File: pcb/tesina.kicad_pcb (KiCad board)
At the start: 2 copper layers, 70 x 35 mm, 73 parts, among them J1 PWR_IN, J2 AMP1_IN, J3 AMP1_OUT2, J4 AMP1_OUT1, J5 AMP2_IN, J6 AMP3_IN, J7 AMP2_OUT, J8 AMP3_OUT, Q1 BFP640, Q2 BFP640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

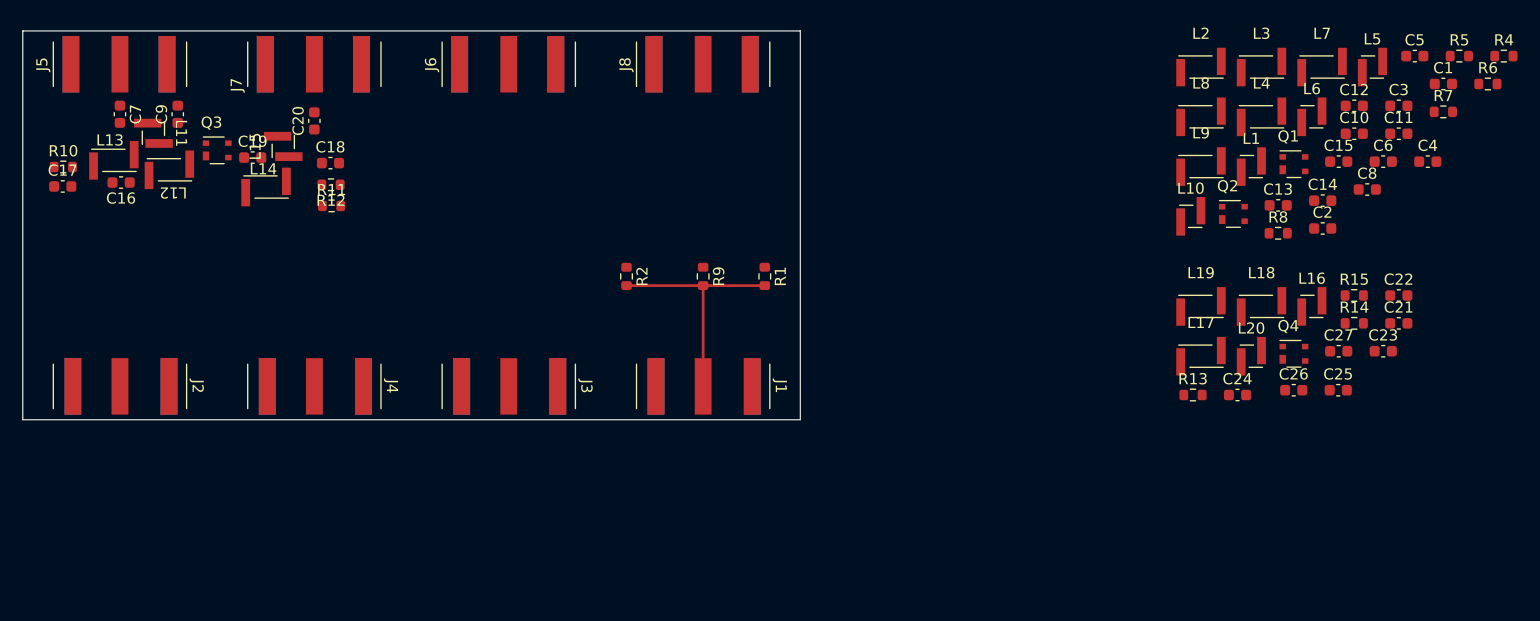
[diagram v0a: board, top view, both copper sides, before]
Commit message: Deleted double stage, updated stub stage, L stage and PCB
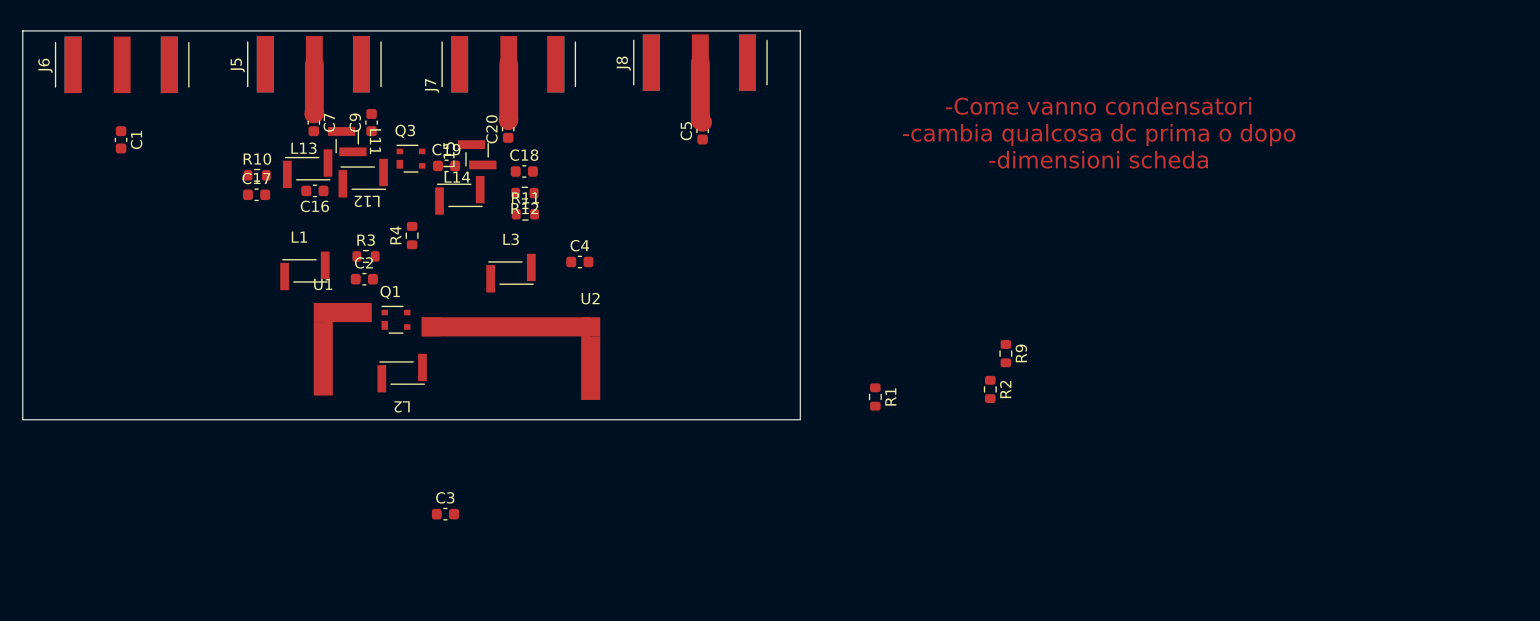
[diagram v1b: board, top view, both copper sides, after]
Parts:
- removed C10, C22: 1.45pF, Capacitor_SMD:C_0603_1608Metric
- removed C11, C12, C13, C15, C21, C23, C24, C25, C27, C8: 100pF, Capacitor_SMD:C_0603_1608Metric
- removed C14, C26, C6: 398fF, Capacitor_SMD:C_0603_1608Metric
- removed J1: PWR_IN, Nicobigio01:Linx_CONSMA003.031-L-G
- removed J2: AMP1_IN, Nicobigio01:Linx_CONSMA003.031-L-G
- removed J3: AMP1_OUT2, Nicobigio01:Linx_CONSMA003.031-L-G
- removed J4: AMP1_OUT1, Nicobigio01:Linx_CONSMA003.031-L-G
- removed L10, L20, L5: 1.78nH, Nicobigio01:Coilcraft_0906-xxLx
- removed L16, L6: 1.26nH, Nicobigio01:Coilcraft_0906-xxLx
- removed L17, L18, L19, L4, L7, L8, L9: 7.15nH, Nicobigio01:Coilcraft_1606-xxLx
- removed Q2, Q4: BFP640, Nicobigio01:SOT-343
- removed R13, R6: Ω, Resistor_SMD:R_0603_1608Metric
- removed R14, R7: 44kΩ, Resistor_SMD:R_0603_1608Metric
- removed R15, R5, R8: 375Ω, Resistor_SMD:R_0603_1608Metric
- added R3: 44kΩ, Resistor_SMD:R_0603_1608Metric, F.Cu at (113.7, 92.1)
- added U1: Single_Stub_Input, Nicobigio01:Microwave_Single_Stub_Input, F.Cu at (109.8, 97.2)
- added U2: Single_Stub_Output, Nicobigio01:Microwave_SIngle_Stub_Output, F.Cu at (133.9, 98.4)
- C2: value 1.45pF -> 100pF
- L1: value 1.26nH -> 7.15nH; footprint Nicobigio01:Coilcraft_0906-xxLx -> Nicobigio01:Coilcraft_1606-xxLx
- R1: value 0Ω -> Ω
- R4: value 44kΩ -> 375Ω
- moved C1 119.1 mm to (91.7, 81.6), turned to -90 degrees
- moved R4 99.6 mm to (117.8, 90.2), turned to 90 degrees
- moved C3 93.4 mm to (120.8, 115.3)
- moved C2 86.4 mm to (113.5, 94.2)
- moved L1 85.7 mm to (108.2, 93.4)
- moved Q1 82.0 mm to (116.4, 97.8)
- moved L2 77.0 mm to (117.0, 102.6), turned to 180 degrees
- moved C4 76.9 mm to (132.9, 92.6)
- moved L3 70.1 mm to (126.8, 93.6)
- moved C5 64.5 mm to (144.0, 80.8), turned to 90 degrees
- moved J6 34.8 mm to (91.8, 74.8)
- moved R2 34.3 mm to (169.9, 104.1)
- moved R9 28.1 mm to (171.3, 100.8)
- moved J5 17.5 mm to (109.0, 74.8)
- moved J7 17.5 mm to (126.5, 74.8)
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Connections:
- net /Amplifier2/STAGE1_IN renamed /Amplifier2/RF2_IN
- net /Amplifier2/STAGE2_OUT renamed /Amplifier2/RF2_OUT
- net Net-(C17-Pad1) renamed /Amplifier2/DC3
- net Net-(C18-Pad1) renamed /Amplifier2/DC1
- net Net-(C19-Pad1) renamed /Amplifier2/RF2_OUT_BM
- net Net-(L12-Pad1) renamed /Amplifier2/RF2_IN_AM
- C1 pad 1: /Amplificatore1/STAGE1_IN -> /Amplifier1/RF1_IN
- C1 pad 2: Net-(C1-Pad2) -> /Amplifier1/RF1_IN_BM
- C2 pad 1: Net-(C1-Pad2) -> Net-(C2-Pad1)
- C4 pad 1: Net-(C4-Pad1) -> /Amplifier1/DC1
- C5 pad 1: Net-(C5-Pad1) -> /Amplifier1/RF1_OUT_AM
- C5 pad 2: GND -> /Amplifier1/RF1_OUT
- J6 pad 1: /Amplifier3/STAGE1_IN -> /Amplifier1/RF1_IN
- J8 pad 1: /Amplifier3/STAGE2_OUT -> /Amplifier1/RF1_OUT
- L1 pad 1: Net-(C1-Pad2) -> /Amplifier1/RF1_IN_BM
- L1 pad 2: Net-(L1-Pad2) -> Net-(C2-Pad1)
- L2 pad 1: Net-(L1-Pad2) -> Net-(C3-Pad1)
- L2 pad 2: Net-(C3-Pad1) -> /Amplifier1/RF1_IN_BM
- L3 pad 1: Net-(C4-Pad1) -> /Amplifier1/RF1_OUT_BF
- L3 pad 2: Net-(L1-Pad2) -> /Amplifier1/DC1
- Q1 pad 1: Net-(L1-Pad2) -> Net-(Q1-Pad1)
- Q1 pad 3: Net-(C6-Pad1) -> /Amplifier1/RF1_OUT_BF
- R1 pad 1: /Amplificatore1/VCC -> Net-(C3-Pad1)
- R1 pad 2: Net-(J1-Pad1) -> GND
- R2 pad 2: Net-(J1-Pad1) -> /DC
- R4 pad 1: Net-(C3-Pad1) -> /Amplifier1/VCC
- R4 pad 2: Net-(C5-Pad1) -> /Amplifier1/DC1
- R9 pad 1: /Amplifier3/VCC -> /Amplifier1/VCC
- R9 pad 2: Net-(J1-Pad1) -> /DC
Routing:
- net Net-(J1-Pad1): track 21.6 -> 0.00 mm
- net /Amplifier1/RF1_OUT: track 0.00 -> 5.46 mm
- net /Amplifier2/RF2_OUT: track 0.00 -> 5.10 mm
- net /Amplifier2/RF2_IN: track 0.00 -> 4.50 mm
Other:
- board text added: "-Come vanno condensatori -cambia qualcosa dc prima o dopo -dimensioni scheda"

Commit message: Started PCB Layout
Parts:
- moved R1 65.2 mm to (97.4, 85.2), turned to 0 degrees
- moved C4 46.1 mm to (87.3, 98.8), turned to 180 degrees
- moved C3 36.8 mm to (97.3, 87.0)
- moved C5 35.0 mm to (109.0, 80.4)
- moved J8 34.8 mm to (109.0, 75.3)
- moved R4 32.3 mm to (87.2, 100.4), turned to 0 degrees
- moved U2 31.5 mm to (105.7, 84.5), turned to 45 degrees
- moved R3 27.0 mm to (87.2, 97.2)
- moved C2 26.4 mm to (87.2, 95.5)
- moved L2 25.6 mm to (94.7, 90.0)
- moved L3 24.3 mm to (102.4, 92.3), turned to -45 degrees
- moved C17 24.3 mm to (128.1, 88.0), turned to 180 degrees
- moved L13 24.2 mm to (132.5, 87.4)
- moved R10 24.2 mm to (128.1, 86.3), turned to 180 degrees
- moved Q1 24.0 mm to (92.6, 95.0)
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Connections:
- net /Amplifier1/DC1 renamed /Amplifier1/DC1_1
- net /Amplifier2/DC1 renamed /Amplifier2/DC2_1
- net /Amplifier2/DC3 renamed /Amplifier2/DC2_3
- net /Amplifier2/RF2_OUT renamed /Amplifier2/STAGE2_OUT
- net Net-(C3-Pad1) renamed /Amplifier1/DC1_3
- C2 pad 1: Net-(C2-Pad1) -> /Amplifier1/DC1_2
- L1 pad 1: /Amplifier1/RF1_IN_BM -> /Amplifier1/DC1_2
- L1 pad 2: Net-(C2-Pad1) -> /Amplifier1/RF1_IN_AM
- L2 pad 2: /Amplifier1/RF1_IN_BM -> /Amplifier1/RF1_IN_AM
- Q1 pad 1: Net-(Q1-Pad1) -> /Amplifier1/RF1_IN_AM
- R3 pad 1: Net-(C2-Pad1) -> /Amplifier1/DC1_2
- U1 pad 2: Net-(Q1-Pad1) -> /Amplifier1/RF1_IN_AM
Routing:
- net /Amplifier1/DC1_1: track 0.00 -> 21.6 mm
- net /Amplifier1/RF1_OUT_BF: track 0.00 -> 9.63 mm
- net /Amplifier2/RF2_IN_AM: track 0.00 -> 9.19 mm
- net Net-(C7-Pad2): track 0.00 -> 8.64 mm
- net /Amplifier1/RF1_IN_BM: track 0.00 -> 7.03 mm
- net /Amplifier2/RF2_OUT_BM: track 0.00 -> 5.49 mm
- net /Amplifier2/DC2_1: track 0.00 -> 5.24 mm
- net Net-(C19-Pad2): track 0.00 -> 5.04 mm
- net /Amplifier1/RF1_IN_AM: track 0.00 -> 4.29 mm
- net /Amplifier1/DC1_3: track 0.00 -> 4.29 mm
- net /Amplifier1/DC1_2: track 0.00 -> 4.09 mm
- net /Amplifier2/DC2_3: track 0.00 -> 3.39 mm
- net /Amplifier1/RF1_IN: track 0.00 -> 3.37 mm
- net /Amplifier1/RF1_OUT_AM: track 0.00 -> 2.94 mm
- net Net-(C16-Pad1): track 0.00 -> 1.74 mm
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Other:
- board text added: "?"

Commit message: backup version before changes
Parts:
- added H1: MountingHole_Pad, MountingHole:MountingHole_2.5mm_Pad_TopBottom, F.Cu at (148.6, 84.2)
- added H2: MountingHole_Pad, MountingHole:MountingHole_2.5mm_Pad_TopBottom, F.Cu at (148.7, 102.8)
- added H2: MountingHole_Pad, MountingHole:MountingHole_2.5mm_Pad_TopBottom, F.Cu at (117.7, 85.0)
- added H2: MountingHole_Pad, MountingHole:MountingHole_2.5mm_Pad_TopBottom, F.Cu at (102.7, 103.0)
- added H3: MountingHole_Pad, MountingHole:MountingHole_2.5mm_Pad_TopBottom, F.Cu at (86.4, 84.4)
- added J1: Conn_01x02_Male, Connector_PinHeader_2.54mm:PinHeader_1x02_P2.54mm_Vertical, F.Cu at (116.7, 100.0)
- moved R9 60.5 mm to (110.8, 100.0), turned to 0 degrees
- moved R2 52.7 mm to (124.8, 100.0), turned to 180 degrees
- moved L3 5.81 mm to (98.5, 96.6)
- moved R11 1.84 mm to (139.3, 92.7)
- moved R12 1.58 mm to (139.3, 94.4)
- moved L2 1.27 mm to (95.1, 88.7)
- moved C3 1.27 mm to (97.7, 85.8)
- moved R1 1.27 mm to (97.8, 84.0)
- moved C1 0.65 mm to (91.6, 80.4)
- moved U2 0.38 mm to (105.6, 84.9)
- moved L1 0.21 mm to (88.5, 92.6)
- turned C4 to 0 degrees
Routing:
- net /DC: track 0.00 -> 16.7 mm
- net Net-(C16-Pad1): track 1.74 -> 11.8 mm
- net GND: track 0.00 -> 4.67 mm, vias 0 -> 61
- net /Amplifier1/DC1_1: track 21.6 -> 17.9 mm
- net /Amplifier1/RF1_IN_AM: track 4.29 -> 6.10 mm
- net /Amplifier1/RF1_OUT_BF: track 9.63 -> 11.4 mm
- net /Amplifier1/RF1_IN: track 3.37 -> 4.37 mm
- added copper zone on B.Cu, net GND
- added copper zone on F.Cu, net GND
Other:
- board text added: "-Come vanno condensatori -cambia qualcosa dc prima o dopo -metal loss e come ottenere tan delta a temp"
- board text added: "filtro grosso pad alimentazione alimentazione anche negativa condenatore parallelo filtro piccolo cambiare fori massa transistor"
- board text removed: "-Come vanno condensatori -cambia qualcosa dc prima o dopo -dimensioni scheda"

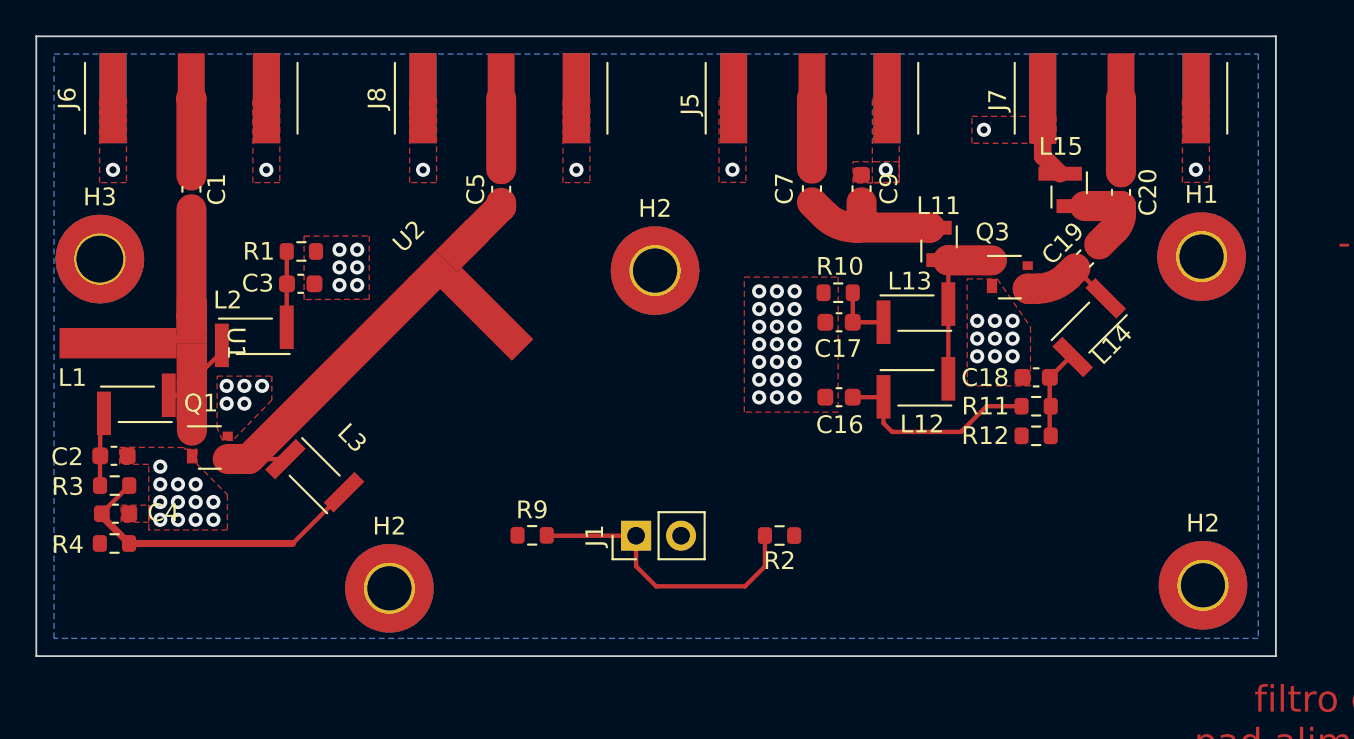
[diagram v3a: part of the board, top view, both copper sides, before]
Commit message: alternate board
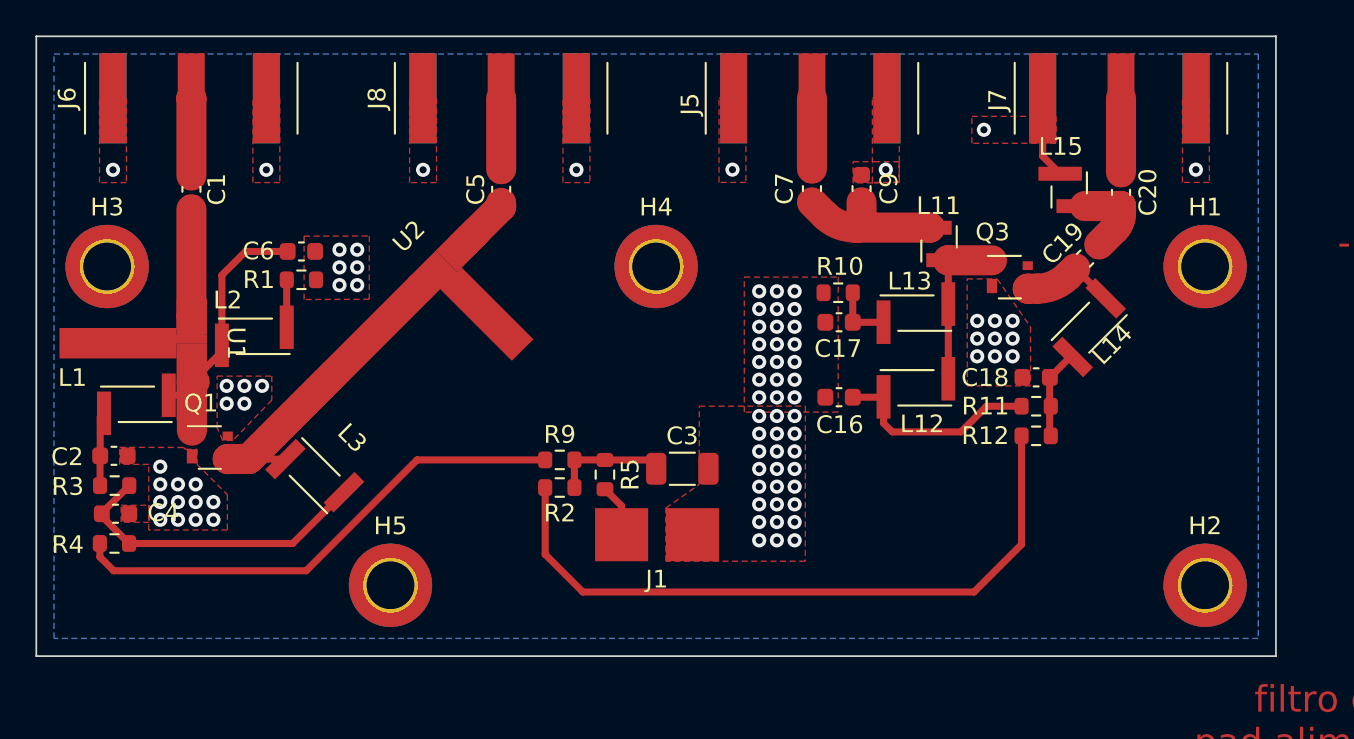
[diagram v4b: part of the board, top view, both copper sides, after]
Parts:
- removed the H2 at (117.7, 85.0)
- removed the H2 at (102.7, 103.0)
- added C6: 100pF, Capacitor_SMD:C_0603_1608Metric, F.Cu at (97.8, 84.0)
- added H4: MountingHole_Pad, MountingHole:MountingHole_2.7mm_M2.5_DIN965_Pad_TopBottom, F.Cu at (117.8, 84.8)
- added H5: MountingHole_Pad, MountingHole:MountingHole_2.7mm_M2.5_DIN965_Pad_TopBottom, F.Cu at (102.8, 102.8)
- added R5: 1Ω, Resistor_SMD:R_0603_1608Metric, F.Cu at (114.9, 96.5)
- C3: value 100pF -> 100nF; footprint Capacitor_SMD:C_0603_1608Metric -> Capacitor_SMD:C_1206_3216Metric
- H1, H2, H3: footprint MountingHole:MountingHole_2.5mm_Pad_TopBottom -> MountingHole:MountingHole_2.7mm_M2.5_DIN965_Pad_TopBottom
- J1: footprint Connector_PinHeader_2.54mm:PinHeader_1x02_P2.54mm_Vertical -> Nicobigio01:Connector_Pad
- moved C3 23.9 mm to (119.3, 96.2)
- moved R2 12.7 mm to (112.4, 97.3), turned to 0 degrees
- moved R9 4.54 mm to (112.4, 95.7)
- moved R1 1.60 mm to (97.8, 85.5)
- moved J1 1.18 mm to (117.9, 99.9), turned to 0 degrees
- moved H1 0.59 mm to (148.8, 84.8)
- moved H3 0.59 mm to (86.8, 84.8)
- moved H2 0.12 mm to (148.8, 102.8)
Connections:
- C3 pad 1: /Amplifier1/DC1_3 -> /DC
- J1 pad 1: /DC -> Net-(J1-Pad1)
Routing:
- net /Amplifier2/VCC: track 0.00 -> 38.8 mm
- net /Amplifier1/VCC: track 0.00 -> 28.8 mm
- net /DC: track 16.7 -> 6.39 mm
- net /Amplifier1/RF1_IN_AM: track 6.10 -> 14.3 mm
- net Net-(J1-Pad1): track 0.00 -> 2.96 mm
- net /Amplifier1/DC1_3: track 4.25 -> 2.44 mm
- net GND: vias 61 -> 85
